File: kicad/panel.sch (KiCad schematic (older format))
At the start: 8 parts, among them CON21 Panel1, CON22 Panel2, CON5 AUX, SW1 SW_PUSH, U2 SN74HCT245PW

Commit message: Place
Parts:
- SW1: value SW_PUSH -> RESET
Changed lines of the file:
@@
 D13
 $Comp
-L GND #PWR050
+L GND #PWR55
 U 1 1 534EE36C
 P 2000 2250
-F 0 "#PWR050" H 2000 2250 30  0001 C CNN
+F 0 "#PWR55" H 2000 2250 30  0001 C CNN
 F 1 "GND" H 2000 2180 30  0001 C CNN
 F 2 "~" H 2000 2250 60  0000 C CNN
@@
 P 2950 1750
 F 0 "SW1" H 3100 1860 50  0000 C CNN
-F 1 "SW_PUSH" H 2950 1670 50  0000 C CNN
+F 1 "RESET" H 2950 1670 50  0000 C CNN
 F 2 "PIN2" H 2950 1600 40  0000 C CNN
 F 3 "" H 2950 1750 60  0000 C CNN
@@
 $EndComp
 $Comp
-L GND #PWR051
+L GND #PWR54
 U 1 1 536AA50B
 P 2950 2150
-F 0 "#PWR051" H 2950 2150 30  0001 C CNN
+F 0 "#PWR54" H 2950 2150 30  0001 C CNN
 F 1 "GND" H 2950 2080 30  0001 C CNN
 F 2 "~" H 2950 2150 60  0000 C CNN
@@
 	5650 1500 5250 1500
 $Comp
-L GND #PWR052
+L GND #PWR53
 U 1 1 538CDD99
 P 5550 2000
-F 0 "#PWR052" H 5550 2000 30  0001 C CNN
+F 0 "#PWR53" H 5550 2000 30  0001 C CNN
 F 1 "GND" H 5550 1930 30  0001 C CNN
 F 2 "~" H 5550 2000 60  0000 C CNN
@@
 $EndComp
 $Comp
-L GND #PWR053
+L GND #PWR59
 U 1 1 538E32BE
 P 3450 4350
-F 0 "#PWR053" H 3450 4350 30  0001 C CNN
+F 0 "#PWR59" H 3450 4350 30  0001 C CNN
 F 1 "GND" H 3450 4280 30  0001 C CNN
 F 2 "" H 3450 4350 60  0000 C CNN
@@
 	3200 3950 3650 3950
 $Comp
-L GND #PWR054
+L GND #PWR58
 U 1 1 538E3349
 P 3250 4350
-F 0 "#PWR054" H 3250 4350 30  0001 C CNN
+F 0 "#PWR58" H 3250 4350 30  0001 C CNN
 F 1 "GND" H 3250 4280 30  0001 C CNN
 F 2 "" H 3250 4350 60  0000 C CNN
@@
 	2500 4050 2300 4050
 $Comp
-L GND #PWR055
+L GND #PWR57
 U 1 1 538E301C
 P 2400 4350
-F 0 "#PWR055" H 2400 4350 30  0001 C CNN
+F 0 "#PWR57" H 2400 4350 30  0001 C CNN
 F 1 "GND" H 2400 4280 30  0001 C CNN
 F 2 "" H 2400 4350 60  0000 C CNN
@@
 Connection ~ 6150 3800
 $Comp
-L GND #PWR056
+L GND #PWR56
 U 1 1 539474AA
 P 6150 4200
-F 0 "#PWR056" H 6150 4200 30  0001 C CNN
+F 0 "#PWR56" H 6150 4200 30  0001 C CNN
 F 1 "GND" H 6150 4130 30  0001 C CNN
 F 2 "" H 6150 4200 60  0000 C CNN

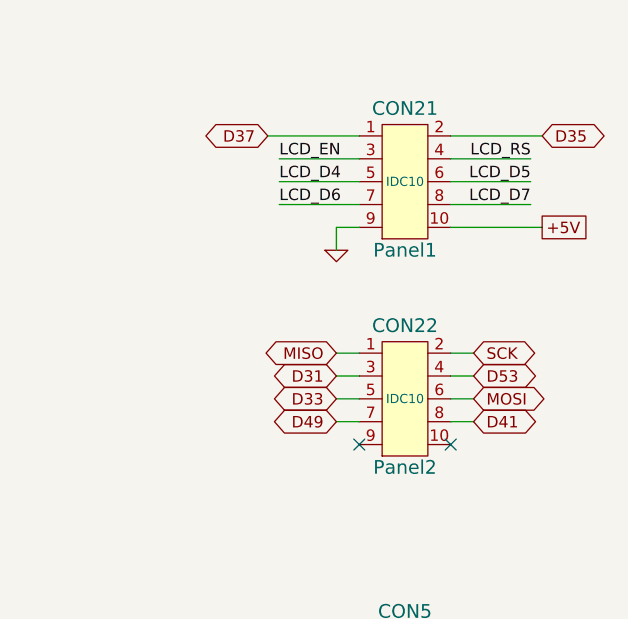
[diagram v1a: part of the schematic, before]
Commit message: Fix panel connections. Place.
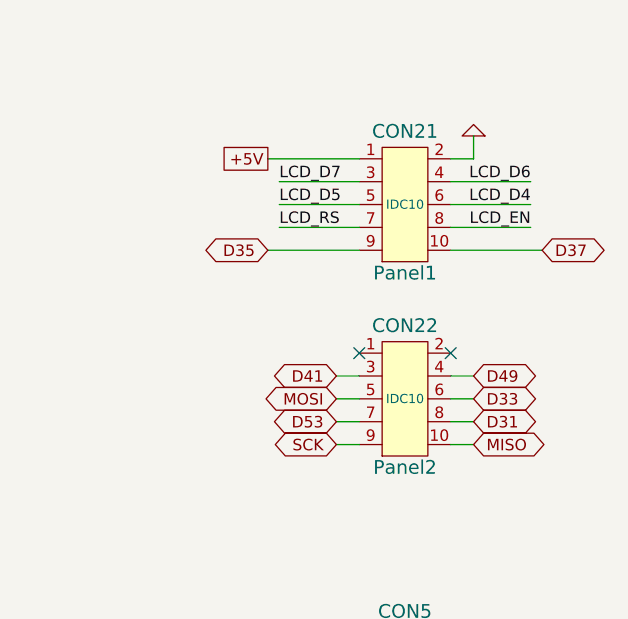
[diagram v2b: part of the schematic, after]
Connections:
- net +5V: now also CON21.1; no longer CON21.10
- net D31: now also CON22.8; no longer CON22.3
- net D33: now also CON22.6; no longer CON22.5
- net D35: now also CON21.9; no longer CON21.2
- net D37: now also CON21.10; no longer CON21.1
- net D41: now also CON22.3; no longer CON22.8
- net D49: now also CON22.4; no longer CON22.7
- net D53: now also CON22.7; no longer CON22.4
- net GND: now also CON21.2; no longer CON21.9
- net LCD_D4: now also CON21.6; no longer CON21.5
- net LCD_D5: now also CON21.5; no longer CON21.6
- net LCD_D6: now also CON21.4; no longer CON21.7
- net LCD_D7: now also CON21.3; no longer CON21.8
- net LCD_EN: now also CON21.8; no longer CON21.3
- net LCD_RS: now also CON21.7; no longer CON21.4
- net MISO: now also CON22.10; no longer CON22.1
- net MOSI: now also CON22.5; no longer CON22.6
- net SCK: now also CON22.9; no longer CON22.2
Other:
- moved on the sheet: CON21
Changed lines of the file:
@@
 D13
 $Comp
-L GND #PWR55
+L GND #PWR053
 U 1 1 534EE36C
 P 2000 2250
-F 0 "#PWR55" H 2000 2250 30  0001 C CNN
+F 0 "#PWR053" H 2000 2250 30  0001 C CNN
 F 1 "GND" H 2000 2180 30  0001 C CNN
 F 2 "~" H 2000 2250 60  0000 C CNN
@@
 $EndComp
 $Comp
-L GND #PWR54
+L GND #PWR054
 U 1 1 536AA50B
 P 2950 2150
-F 0 "#PWR54" H 2950 2150 30  0001 C CNN
+F 0 "#PWR054" H 2950 2150 30  0001 C CNN
 F 1 "GND" H 2950 2080 30  0001 C CNN
 F 2 "~" H 2950 2150 60  0000 C CNN
@@
 	0    -1   1    0
 $EndComp
-Text GLabel 6450 1500 2    50   BiDi ~ 0
+Text GLabel 5250 2000 0    50   BiDi ~ 0
 D35
-Text GLabel 5250 1500 0    50   BiDi ~ 0
+Text GLabel 6450 2000 2    50   BiDi ~ 0
 D37
 $Comp
 L CON5x2 CON21
 U 1 1 538CD96D
-P 5850 1700
-F 0 "CON21" H 5850 2020 60  0000 C CNN
-F 1 "Panel1" H 5850 1400 60  0000 C CNN
-F 2 "IDC10" H 5850 1700 40  0000 C CNN
-F 3 "" H 5850 1700 40  0000 C CNN
-	1    5850 1700
+P 5850 1800
+F 0 "CON21" H 5850 2120 60  0000 C CNN
+F 1 "Panel1" H 5850 1500 60  0000 C CNN
+F 2 "IDC10" H 5850 1800 40  0000 C CNN
+F 3 "" H 5850 1800 40  0000 C CNN
+	1    5850 1800
 	1    0    0    -1
 $EndComp
@@
 	2950 2150 2950 2050
 Wire Wire Line
-	6450 1500 6050 1500
-Wire Wire Line
-	6050 1600 6400 1600
+	5250 2000 5650 2000
+Wire Wire Line
+	5650 1900 5300 1900
+Wire Wire Line
+	5300 1800 5650 1800
+Wire Wire Line
+	5650 1700 5300 1700
+Wire Wire Line
+	5250 1600 5650 1600
+Wire Wire Line
+	6150 1600 6050 1600
 Wire Wire Line
 	6400 1700 6050 1700
 Wire Wire Line
-	6050 1800 6400 1800
-Wire Wire Line
-	6450 1900 6050 1900
-Wire Wire Line
-	5550 1900 5650 1900
-Wire Wire Line
-	5300 1800 5650 1800
-Wire Wire Line
-	5300 1700 5650 1700
-Wire Wire Line
-	5650 1600 5300 1600
-Wire Wire Line
-	5650 1500 5250 1500
-$Comp
-L GND #PWR53
+	6400 1800 6050 1800
+Wire Wire Line
+	6050 1900 6400 1900
+Wire Wire Line
+	6050 2000 6450 2000
+$Comp
+L GND #PWR055
 U 1 1 538CDD99
-P 5550 2000
-F 0 "#PWR53" H 5550 2000 30  0001 C CNN
-F 1 "GND" H 5550 1930 30  0001 C CNN
-F 2 "~" H 5550 2000 60  0000 C CNN
-F 3 "~" H 5550 2000 60  0000 C CNN
-	1    5550 2000
-	1    0    0    -1
-$EndComp
-Wire Wire Line
-	5550 1900 5550 2000
+P 6150 1500
+F 0 "#PWR055" H 6150 1500 30  0001 C CNN
+F 1 "GND" H 6150 1430 30  0001 C CNN
+F 2 "~" H 6150 1500 60  0000 C CNN
+F 3 "~" H 6150 1500 60  0000 C CNN
+	1    6150 1500
+	-1   0    0    1
+$EndComp
+Wire Wire Line
+	6150 1600 6150 1500
+Text GLabel 5550 2650 0    50   BiDi ~ 0
+MOSI
+Text GLabel 6150 2750 2    50   BiDi ~ 0
+D31
 Text GLabel 6150 2650 2    50   BiDi ~ 0
-MOSI
+D33
+Text GLabel 5250 1600 0    50   UnSpc ~ 0
++5V
+Wire Wire Line
+	6150 2550 6050 2550
+Wire Wire Line
+	6150 2650 6050 2650
+Wire Wire Line
+	6050 2750 6150 2750
+Wire Wire Line
+	6050 2850 6150 2850
+Text GLabel 5550 2750 0    50   BiDi ~ 0
+D53
+Text GLabel 5550 2850 0    50   BiDi ~ 0
+SCK
+Text GLabel 6150 2850 2    50   BiDi ~ 0
+MISO
 Text GLabel 5550 2550 0    50   BiDi ~ 0
-D31
-Text GLabel 5550 2650 0    50   BiDi ~ 0
-D33
-Text GLabel 6450 1900 2    50   UnSpc ~ 0
-+5V
-Wire Wire Line
-	5550 2750 5650 2750
+D41
+Wire Wire Line
+	5550 2850 5650 2850
+Wire Wire Line
+	5650 2750 5550 2750
 Wire Wire Line
 	5550 2650 5650 2650
 Wire Wire Line
 	5650 2550 5550 2550
-Wire Wire Line
-	5650 2450 5550 2450
+NoConn ~ 5650 2450
+NoConn ~ 6050 2450
 Text GLabel 6150 2550 2    50   BiDi ~ 0
-D53
-Text GLabel 6150 2450 2    50   BiDi ~ 0
-SCK
-Text GLabel 5550 2450 0    50   BiDi ~ 0
-MISO
-Text GLabel 6150 2750 2    50   BiDi ~ 0
-D41
-Wire Wire Line
-	6150 2450 6050 2450
-Wire Wire Line
-	6050 2550 6150 2550
-Wire Wire Line
-	6150 2650 6050 2650
-Wire Wire Line
-	6050 2750 6150 2750
-NoConn ~ 6050 2850
-NoConn ~ 5650 2850
-Text GLabel 5550 2750 0    50   BiDi ~ 0
 D49
 $Comp
@@
 $EndComp
 $Comp
-L GND #PWR59
+L GND #PWR056
 U 1 1 538E32BE
 P 3450 4350
-F 0 "#PWR59" H 3450 4350 30  0001 C CNN
+F 0 "#PWR056" H 3450 4350 30  0001 C CNN
 F 1 "GND" H 3450 4280 30  0001 C CNN
 F 2 "" H 3450 4350 60  0000 C CNN
@@
 	3200 3950 3650 3950
 $Comp
-L GND #PWR58
+L GND #PWR057
 U 1 1 538E3349
 P 3250 4350
-F 0 "#PWR58" H 3250 4350 30  0001 C CNN
+F 0 "#PWR057" H 3250 4350 30  0001 C CNN
 F 1 "GND" H 3250 4280 30  0001 C CNN
 F 2 "" H 3250 4350 60  0000 C CNN
@@
 	2500 4050 2300 4050
 $Comp
-L GND #PWR57
+L GND #PWR058
 U 1 1 538E301C
 P 2400 4350
-F 0 "#PWR57" H 2400 4350 30  0001 C CNN
+F 0 "#PWR058" H 2400 4350 30  0001 C CNN
 F 1 "GND" H 2400 4280 30  0001 C CNN
 F 2 "" H 2400 4350 60  0000 C CNN
@@
 Wire Wire Line
 	2350 3550 2500 3550
-Text Label 5300 1600 0    50   ~ 0
+Text Label 6400 1900 2    50   ~ 0
 LCD_EN
+Text Label 6400 1800 2    50   ~ 0
+LCD_D4
+Text Label 6400 1700 2    50   ~ 0
+LCD_D6
+Text Label 5300 1900 0    50   ~ 0
+LCD_RS
+Text Label 5300 1800 0    50   ~ 0
+LCD_D5
 Text Label 5300 1700 0    50   ~ 0
-LCD_D4
-Text Label 5300 1800 0    50   ~ 0
-LCD_D6
-Text Label 6400 1600 2    50   ~ 0
-LCD_RS
-Text Label 6400 1700 2    50   ~ 0
-LCD_D5
-Text Label 6400 1800 2    50   ~ 0
 LCD_D7
 Text Label 3600 3050 2    50   ~ 0
@@
 Connection ~ 6150 3800
 $Comp
-L GND #PWR56
+L GND #PWR059
 U 1 1 539474AA
 P 6150 4200
-F 0 "#PWR56" H 6150 4200 30  0001 C CNN
+F 0 "#PWR059" H 6150 4200 30  0001 C CNN
 F 1 "GND" H 6150 4130 30  0001 C CNN
 F 2 "" H 6150 4200 60  0000 C CNN

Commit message: Route.
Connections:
- net D23: now also U2.7 (A6); no longer U2.4 (A3)
- net D25: now also U2.6 (A5); no longer U2.5 (A4)
- net D27: now also U2.5 (A4); no longer U2.6 (A5)
- net D29: now also U2.4 (A3); no longer U2.7 (A6)
- net LCD_D4: now also U2.13 (B6); no longer U2.16 (B3)
- net LCD_D5: now also U2.14 (B5); no longer U2.15 (B4)
- net LCD_D6: now also U2.15 (B4); no longer U2.14 (B5)
- net LCD_D7: now also U2.16 (B3); no longer U2.13 (B6)
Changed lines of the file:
@@
 Text GLabel 2350 3050 0    50   BiDi ~ 0
 D17
-Text GLabel 2350 3250 0    50   BiDi ~ 0
+Text GLabel 2350 3550 0    50   BiDi ~ 0
 D23
-Text GLabel 2350 3450 0    50   BiDi ~ 0
+Text GLabel 2350 3350 0    50   BiDi ~ 0
 D27
 Text GLabel 2350 3150 0    50   BiDi ~ 0
 D16
-Text GLabel 2350 3350 0    50   BiDi ~ 0
+Text GLabel 2350 3450 0    50   BiDi ~ 0
 D25
-Text GLabel 2350 3550 0    50   BiDi ~ 0
+Text GLabel 2350 3250 0    50   BiDi ~ 0
 D29
 Wire Wire Line
@@
 	2350 3150 2500 3150
 Wire Wire Line
+	2350 3550 2500 3550
+Wire Wire Line
+	2350 3450 2500 3450
+Wire Wire Line
+	2350 3350 2500 3350
+Wire Wire Line
 	2350 3250 2500 3250
-Wire Wire Line
-	2350 3350 2500 3350
-Wire Wire Line
-	2350 3450 2500 3450
-Wire Wire Line
-	2350 3550 2500 3550
 Text Label 6400 1900 2    50   ~ 0
 LCD_EN
@@
 Text Label 3600 3050 2    50   ~ 0
 LCD_EN
-Text Label 3600 3250 2    50   ~ 0
+Text Label 3600 3550 2    50   ~ 0
 LCD_D4
-Text Label 3600 3450 2    50   ~ 0
+Text Label 3600 3350 2    50   ~ 0
 LCD_D6
 Text Label 3600 3150 2    50   ~ 0
 LCD_RS
-Text Label 3600 3350 2    50   ~ 0
+Text Label 3600 3450 2    50   ~ 0
 LCD_D5
-Text Label 3600 3550 2    50   ~ 0
+Text Label 3600 3250 2    50   ~ 0
 LCD_D7
 Wire Wire Line
@@
 	3600 3150 3200 3150
 Wire Wire Line
-	3200 3250 3600 3250
-Wire Wire Line
-	3600 3350 3200 3350
-Wire Wire Line
-	3200 3450 3600 3450
-Wire Wire Line
-	3600 3550 3200 3550
+	3200 3550 3600 3550
+Wire Wire Line
+	3600 3450 3200 3450
+Wire Wire Line
+	3200 3350 3600 3350
+Wire Wire Line
+	3600 3250 3200 3250
 Wire Wire Line
 	2500 3650 2400 3650

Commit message: Route.
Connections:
- net D32: now also CON5.9; no longer CON5.1
- net D39: now also CON5.7; no longer CON5.3
- net D42: now also CON5.1; no longer CON5.7
- net D43: now also CON5.3; no longer CON5.9
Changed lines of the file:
@@
 	1    0    0    -1
 $EndComp
-Text GLabel 5450 3700 0    50   Output ~ 0
+Text GLabel 5450 4100 0    50   Output ~ 0
 D32
-Text GLabel 5450 3800 0    50   Output ~ 0
+Text GLabel 5450 4000 0    50   Output ~ 0
 D39
 Text GLabel 5450 3900 0    50   Output ~ 0
 D40
-Text GLabel 5450 4000 0    50   Output ~ 0
+Text GLabel 5450 3700 0    50   Output ~ 0
 D42
-Text GLabel 5450 4100 0    50   Output ~ 0
+Text GLabel 5450 3800 0    50   Output ~ 0
 D43
 Wire Wire Line

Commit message: Route.
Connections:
- net +5V: now also U2.2 (A1), U2.3 (A2)
- net D16: now also U2.8 (A7); no longer U2.3 (A2)
- net D17: now also U2.9 (A8); no longer U2.2 (A1)
- net GND: no longer U2.8 (A7), U2.9 (A8)
- net LCD_EN: now also U2.11 (B8); no longer U2.18 (B1)
- net LCD_RS: now also U2.12 (B7); no longer U2.17 (B2)
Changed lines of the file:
@@
 	1    0    0    -1
 $EndComp
-Text GLabel 2350 3050 0    50   BiDi ~ 0
+Text GLabel 2350 3750 0    50   BiDi ~ 0
 D17
 Text GLabel 2350 3550 0    50   BiDi ~ 0
@@
 Text GLabel 2350 3350 0    50   BiDi ~ 0
 D27
-Text GLabel 2350 3150 0    50   BiDi ~ 0
+Text GLabel 2350 3650 0    50   BiDi ~ 0
 D16
 Text GLabel 2350 3450 0    50   BiDi ~ 0
@@
 $EndComp
 Wire Wire Line
-	2400 3650 2400 4350
-Wire Wire Line
 	2400 4150 2500 4150
 Wire Wire Line
-	2350 3050 2500 3050
-Wire Wire Line
-	2350 3150 2500 3150
+	2350 3750 2500 3750
+Wire Wire Line
+	2350 3650 2500 3650
 Wire Wire Line
 	2350 3550 2500 3550
@@
 Text Label 5300 1700 0    50   ~ 0
 LCD_D7
-Text Label 3600 3050 2    50   ~ 0
+Text Label 3600 3750 2    50   ~ 0
 LCD_EN
 Text Label 3600 3550 2    50   ~ 0
@@
 Text Label 3600 3350 2    50   ~ 0
 LCD_D6
-Text Label 3600 3150 2    50   ~ 0
+Text Label 3600 3650 2    50   ~ 0
 LCD_RS
 Text Label 3600 3450 2    50   ~ 0
@@
 LCD_D7
 Wire Wire Line
-	3200 3050 3600 3050
-Wire Wire Line
-	3600 3150 3200 3150
+	3200 3750 3600 3750
+Wire Wire Line
+	3600 3650 3200 3650
 Wire Wire Line
 	3200 3550 3600 3550
@@
 Wire Wire Line
 	3600 3250 3200 3250
-Wire Wire Line
-	2500 3650 2400 3650
-Connection ~ 2400 4150
-Wire Wire Line
-	2500 3750 2400 3750
-Connection ~ 2400 3750
-NoConn ~ 3200 3650
-NoConn ~ 3200 3750
+NoConn ~ 3200 3050
+NoConn ~ 3200 3150
 $Comp
 L CON5x2 CON5
@@
 	1    0    0    -1
 $EndComp
+Wire Wire Line
+	2400 4150 2400 4350
+Text GLabel 2300 3050 0    60   UnSpc ~ 0
++5V
+Wire Wire Line
+	2300 3050 2500 3050
+Wire Wire Line
+	2500 3150 2400 3150
+Wire Wire Line
+	2400 3150 2400 3050
+Connection ~ 2400 3050
 $EndSCHEMATC
